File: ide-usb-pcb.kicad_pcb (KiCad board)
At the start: 2 copper layers, 30 parts, among them J1 Conn_02x20_Odd_Even, J2 STM32F4_Discovery_Header, J3 Screw_Terminal_01x02, J4 USB_B, U1 TXS0108EPW, U2 TXS0108EPW

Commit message: More routing
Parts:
- moved J1 71.0 mm to (127.0, 123.2), turned to 270 degrees
- moved R24 64.1 mm to (127.0, 116.8), turned to 90 degrees
- moved J3 59.5 mm to (54.6, 134.6), turned to 180 degrees
- moved R1 58.9 mm to (104.1, 134.6)
- moved R2 56.1 mm to (91.4, 134.6)
- moved J4 53.6 mm to (41.9, 116.8), turned to 270 degrees
- moved R3 51.4 mm to (104.1, 132.1)
- moved R4 48.5 mm to (91.4, 132.1)
- moved R14 46.8 mm to (119.4, 91.4), turned to 270 degrees
- moved R5 43.8 mm to (104.1, 129.5)
- moved R15 43.3 mm to (116.8, 91.4), turned to 270 degrees
- moved R6 41.0 mm to (91.4, 129.5)
- moved R9 40.3 mm to (99.1, 116.8), turned to 90 degrees
- moved R16 39.7 mm to (114.3, 91.4), turned to 270 degrees
- moved R10 39.5 mm to (96.5, 116.8), turned to 90 degrees
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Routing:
- net /DIOR: track 0.00 -> 111.0 mm
- net /DA1: track 0.00 -> 90.9 mm
- net +3V3: track 109.3 -> 24.7 mm
- net /DA0: track 0.00 -> 84.6 mm
- net /OE: track 0.00 -> 80.6 mm, vias 0 -> 2
- net /DIOW: track 0.00 -> 67.0 mm
- net /RESET: track 81.9 -> 124.4 mm
- net /CS0: track 93.9 -> 58.6 mm
- net /DD7B: track 12.5 -> 46.2 mm
- net /DD9A: track 11.7 -> 43.2 mm
- net /DD15B: track 12.5 -> 43.9 mm
- net /DA2: track 110.8 -> 81.3 mm, vias 0 -> 1
- net /DD10A: track 9.30 -> 37.8 mm
- net /DD14B: track 15.0 -> 42.8 mm
- net /DD7A: track 27.6 -> 0.00 mm
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
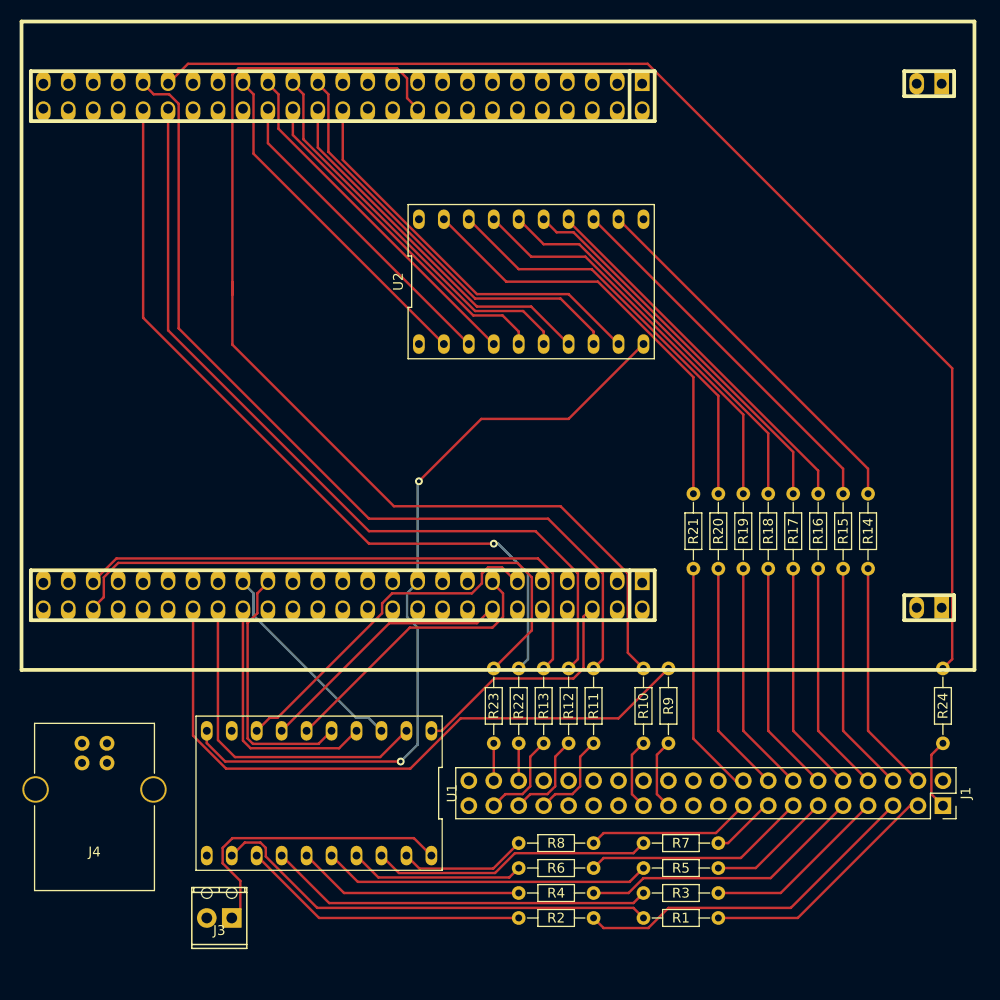
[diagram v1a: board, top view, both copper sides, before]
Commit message: First PCB version with everything routed
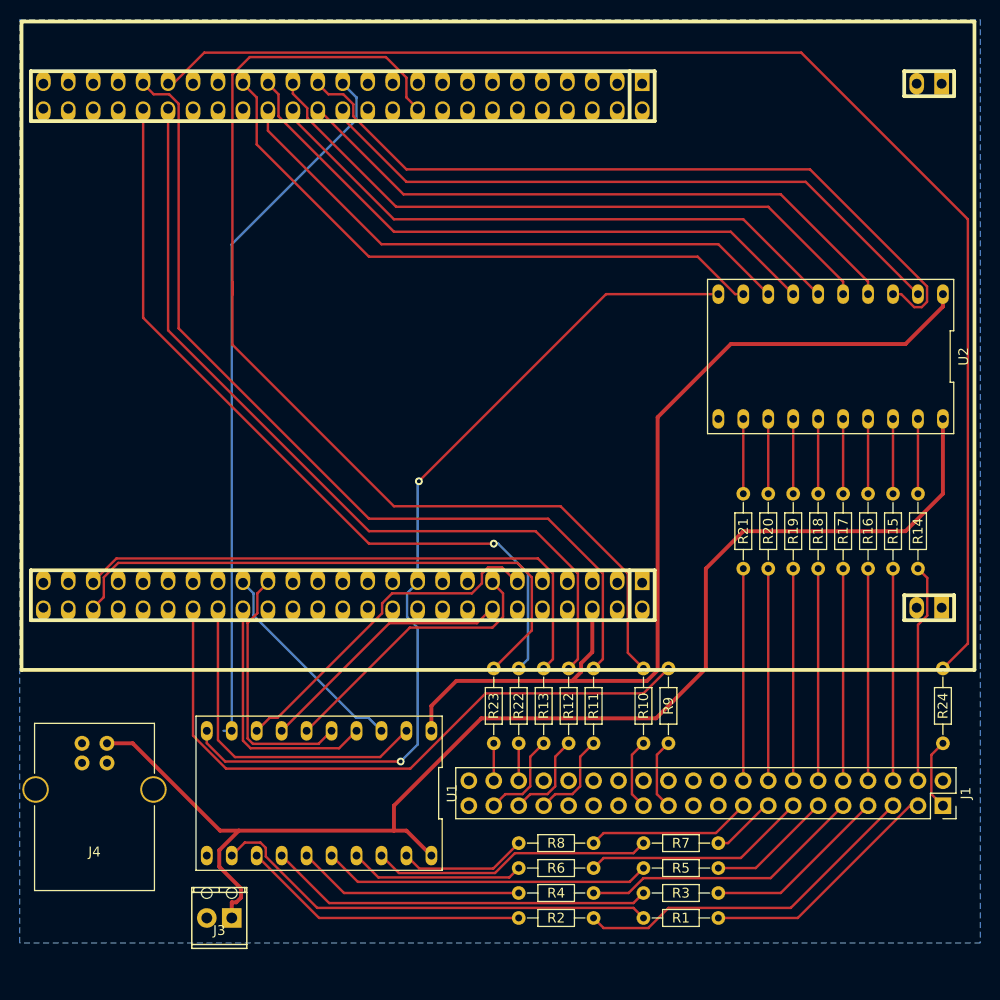
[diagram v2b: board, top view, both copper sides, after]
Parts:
- moved U2 31.4 mm to (115.6, 77.5), turned to 180 degrees
- moved R21 5.08 mm to (106.7, 91.4)
- moved R14 5.08 mm to (124.5, 91.4)
- moved R15 5.08 mm to (121.9, 91.4)
- moved R16 5.08 mm to (119.4, 91.4)
- moved R17 5.08 mm to (116.8, 91.4)
- moved R18 5.08 mm to (114.3, 91.4)
- moved R19 5.08 mm to (111.8, 91.4)
- moved R20 5.08 mm to (109.2, 91.4)
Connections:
- U2 pad 1: /DD15A -> /DD8A
- U2 pad 12: /DD8B -> /DD15B
- U2 pad 13: /DD9B -> /DD14B
- U2 pad 14: /DD10B -> /DD13B
- U2 pad 15: /DD11B -> /DD12B
- U2 pad 16: /DD12B -> /DD11B
- U2 pad 17: /DD13B -> /DD10B
- U2 pad 18: /DD14B -> /DD9B
- U2 pad 20: /DD15B -> /DD8B
- U2 pad 3: /DD14A -> /DD9A
- U2 pad 4: /DD13A -> /DD10A
- U2 pad 5: /DD12A -> /DD11A
- U2 pad 6: /DD11A -> /DD12A
- U2 pad 7: /DD10A -> /DD13A
- U2 pad 8: /DD9A -> /DD14A
- U2 pad 9: /DD8A -> /DD15A
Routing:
- net +5V: track 30.6 -> 134.2 mm
- net /DD7A: track 0.00 -> 72.5 mm
- net +3V3: track 24.7 -> 96.1 mm
- net /DD15B: track 43.9 -> 7.62 mm
- net /DD14B: track 42.8 -> 7.62 mm
- net /DD13B: track 41.7 -> 7.62 mm
- net /DD9A: track 43.2 -> 77.1 mm
- net /DD12B: track 40.6 -> 7.62 mm
- net /DD11B: track 39.5 -> 7.62 mm
- net /DD9B: track 38.5 -> 7.62 mm
- net /DD8B: track 38.5 -> 7.62 mm
- net /DD10B: track 38.5 -> 7.62 mm
- net /DD15A: track 35.0 -> 62.6 mm
- net /DD14A: track 32.4 -> 60.1 mm
- net /DD13A: track 36.0 -> 63.7 mm
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- added copper zone on B.Cu, net GND
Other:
- net class power added: clearance 0.2, trace_width 0.4, via_dia 0.8, via_drill 0.4

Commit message: Fix terminal block footprint
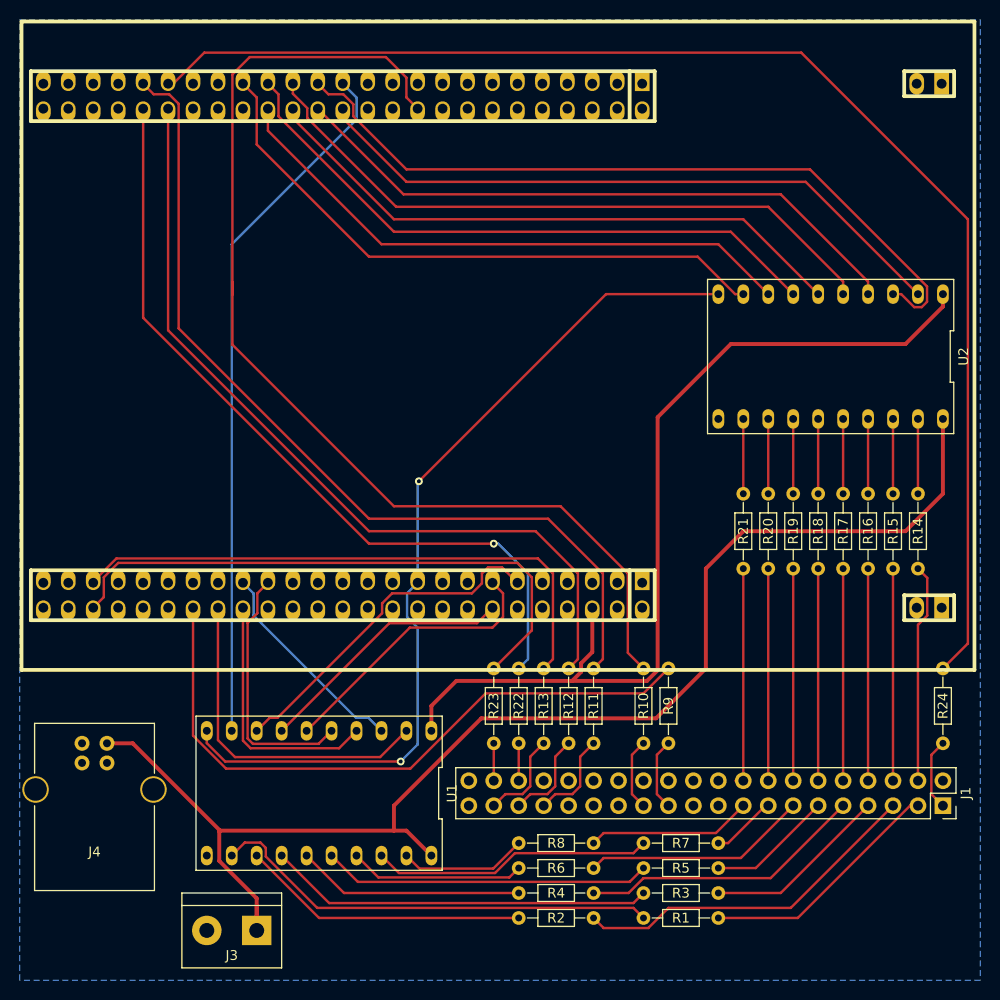
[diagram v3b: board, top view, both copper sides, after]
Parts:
- J3: footprint TerminalBlocks_Phoenix:TerminalBlock_Phoenix_MPT-2.54mm_2pol -> Connectors_Terminal_Blocks:TerminalBlock_bornier-2_P5.08mm
- moved J3 2.84 mm to (57.1, 135.9)
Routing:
- net +5V: track 134.2 -> 135.9 mm
- net /DD7A: track 72.5 -> 71.7 mm

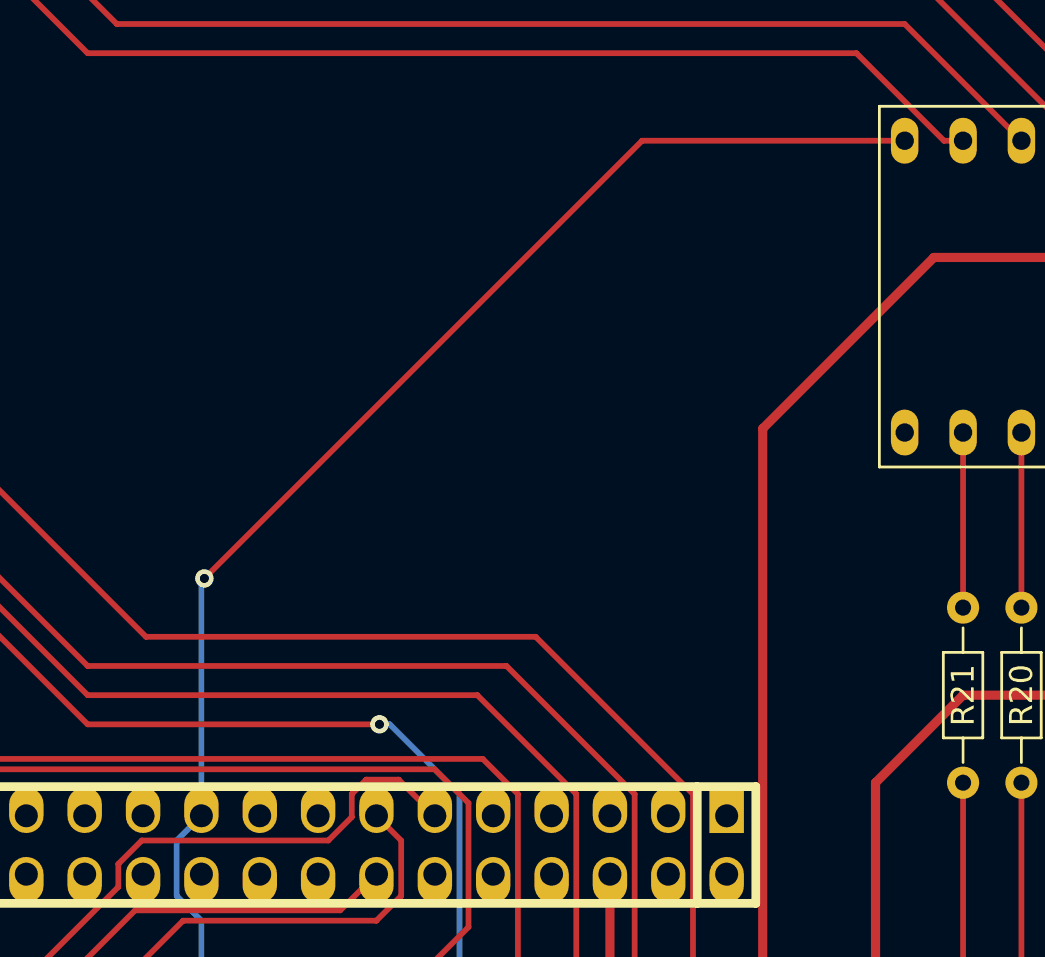
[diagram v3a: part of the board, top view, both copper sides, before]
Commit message: Add OE pulldown resistor
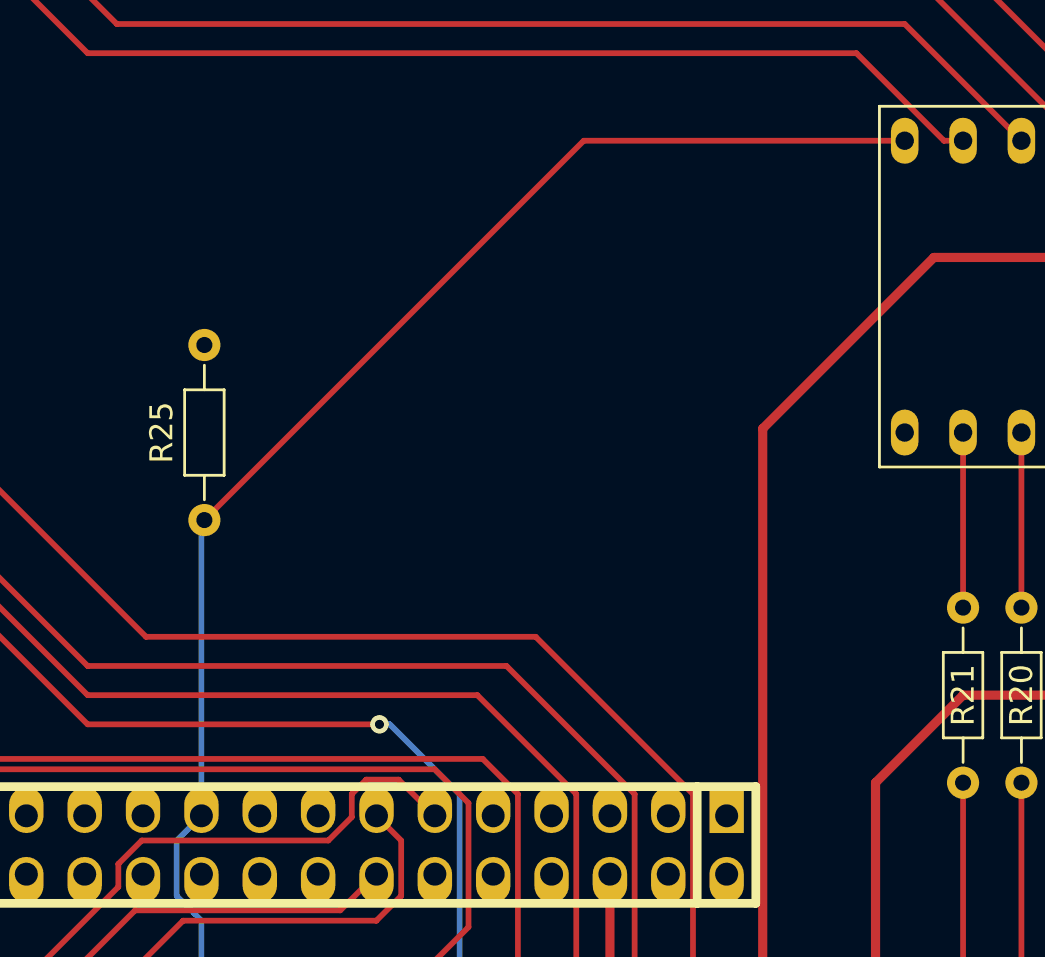
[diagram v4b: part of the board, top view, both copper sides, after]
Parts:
- added R25: 10K, Resistors_THT:R_Axial_DIN0204_L3.6mm_D1.6mm_P7.62mm_Horizontal, F.Cu at (73.7, 87.6)
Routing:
- net /OE: track 90.3 -> 91.8 mm, vias 2 -> 1
